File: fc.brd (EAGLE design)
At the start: 55 x 40 mm, 72 parts, among them IC1 BN055, J1 USBC, U1 LMZ21700, U2 ATMEGA2560-16AU100A-M, U4 FT230XQ, Y1 16MHz, Y2 32.768kHz

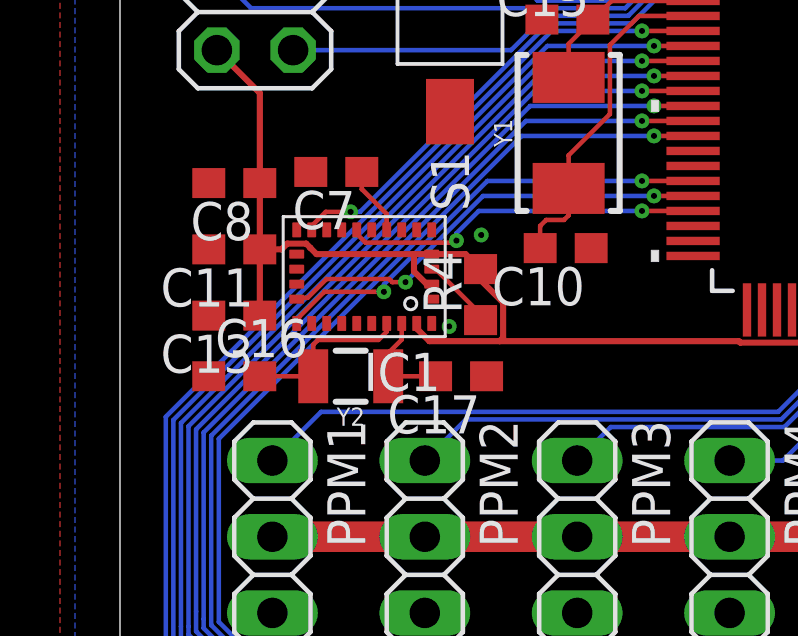
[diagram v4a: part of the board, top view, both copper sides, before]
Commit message: changed caps to sparkfun lib
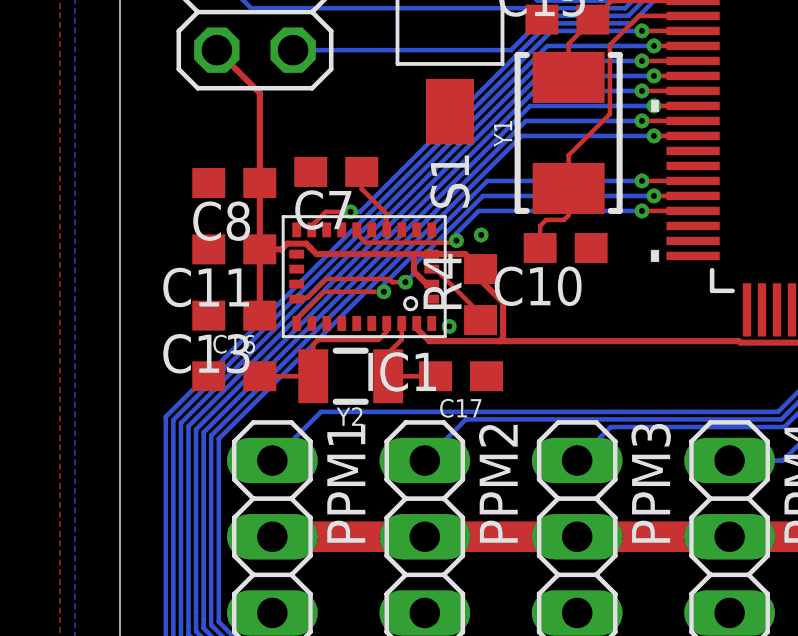
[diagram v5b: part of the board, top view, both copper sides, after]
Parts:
- C10, C12, C15, C4, C5, C6, C9: device rcl:C0603 -> sparkfun-generic-cap:0603
- C11, C13: device resistor:C0603 -> sparkfun-generic-cap:0603
- C16, C17: value 22p -> 22pF; device resistor:C0603 -> SparkFun-Capacitors:0603
- C7, C8: value 100n -> 0.1uF; device resistor:C0603 -> SparkFun-Capacitors:0603

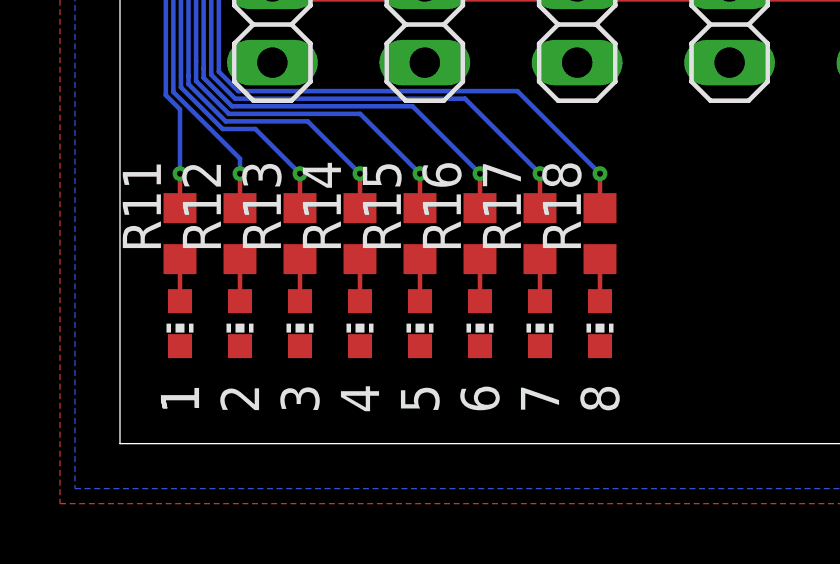
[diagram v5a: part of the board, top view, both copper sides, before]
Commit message: changed LEDs to sparkfun lib
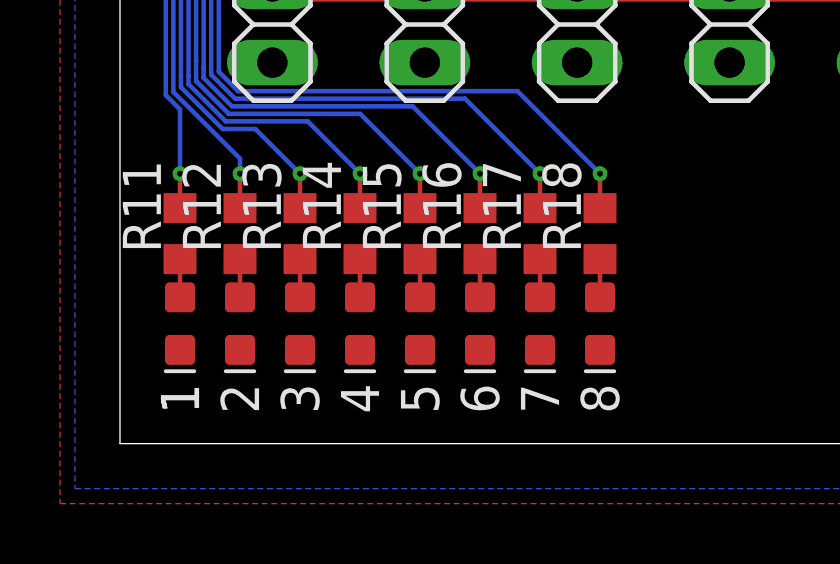
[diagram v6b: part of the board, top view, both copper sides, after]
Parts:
- LED1, LED2, LED3, LED4, LED5, LED6, LED7, LED8: device led:CHIP-LED0603 -> SparkFun-LED:LED-0603
- turned LED1 to 270 degrees
- turned LED2 to 270 degrees
- turned LED3 to 270 degrees
- turned LED4 to 270 degrees
- turned LED5 to 270 degrees
- turned LED6 to 270 degrees
- turned LED7 to 270 degrees
- turned LED8 to 270 degrees
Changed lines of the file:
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@@
 <attribute name="VALUE" x="7.905" y="6.365" size="1.27" layer="27" rot="R90"/>
 </element>
-<element name="LED1" library="led" library_urn="urn:adsk.eagle:library:259" package="CHIP-LED0603" package3d_urn="urn:adsk.eagle:package:15819/3" value="" x="2" y="4" smashed="yes" rot="R180">
-<attribute name="VALUE" x="0.095" y="4.635" size="1.27" layer="27" rot="R270"/>
+<element name="LED1" library="SparkFun-LED" library_urn="urn:adsk.eagle:library:529" package="LED-0603" package3d_urn="urn:adsk.eagle:package:39354/1" value="" x="2" y="4" smashed="yes" rot="R270">
+<attribute name="VALUE" x="1.365" y="2.095" size="1.27" layer="27"/>
 </element>
 <element name="R12" library="rcl" library_urn="urn:adsk.eagle:library:334" package="R0603" package3d_urn="urn:adsk.eagle:package:23555/2" value="100" x="4" y="7" smashed="yes" rot="R90">
@@
 <attribute name="VALUE" x="5.905" y="6.365" size="1.27" layer="27" rot="R90"/>
 </element>
-<element name="LED2" library="led" library_urn="urn:adsk.eagle:library:259" package="CHIP-LED0603" package3d_urn="urn:adsk.eagle:package:15819/3" value="" x="4" y="4" smashed="yes" rot="R180">
-<attribute name="VALUE" x="2.095" y="4.635" size="1.27" layer="27" rot="R270"/>
+<element name="LED2" library="SparkFun-LED" library_urn="urn:adsk.eagle:library:529" package="LED-0603" package3d_urn="urn:adsk.eagle:package:39354/1" value="" x="4" y="4" smashed="yes" rot="R270">
+<attribute name="VALUE" x="3.365" y="2.095" size="1.27" layer="27"/>
 </element>
 <element name="R13" library="rcl" library_urn="urn:adsk.eagle:library:334" package="R0603" package3d_urn="urn:adsk.eagle:package:23555/2" value="100" x="6" y="7" smashed="yes" rot="R90">
@@
 <attribute name="VALUE" x="7.905" y="6.365" size="1.27" layer="27" rot="R90"/>
 </element>
-<element name="LED3" library="led" library_urn="urn:adsk.eagle:library:259" package="CHIP-LED0603" package3d_urn="urn:adsk.eagle:package:15819/3" value="" x="6" y="4" smashed="yes" rot="R180">
-<attribute name="VALUE" x="4.095" y="4.635" size="1.27" layer="27" rot="R270"/>
+<element name="LED3" library="SparkFun-LED" library_urn="urn:adsk.eagle:library:529" package="LED-0603" package3d_urn="urn:adsk.eagle:package:39354/1" value="" x="6" y="4" smashed="yes" rot="R270">
+<attribute name="VALUE" x="5.365" y="2.095" size="1.27" layer="27"/>
 </element>
 <element name="R14" library="rcl" library_urn="urn:adsk.eagle:library:334" package="R0603" package3d_urn="urn:adsk.eagle:package:23555/2" value="100" x="8" y="7" smashed="yes" rot="R90">
@@
 <attribute name="VALUE" x="9.905" y="6.365" size="1.27" layer="27" rot="R90"/>
 </element>
-<element name="LED4" library="led" library_urn="urn:adsk.eagle:library:259" package="CHIP-LED0603" package3d_urn="urn:adsk.eagle:package:15819/3" value="" x="8" y="4" smashed="yes" rot="R180">
-<attribute name="VALUE" x="6.095" y="4.635" size="1.27" layer="27" rot="R270"/>
+<element name="LED4" library="SparkFun-LED" library_urn="urn:adsk.eagle:library:529" package="LED-0603" package3d_urn="urn:adsk.eagle:package:39354/1" value="" x="8" y="4" smashed="yes" rot="R270">
+<attribute name="VALUE" x="7.365" y="2.095" size="1.27" layer="27"/>
 </element>
 <element name="R15" library="rcl" library_urn="urn:adsk.eagle:library:334" package="R0603" package3d_urn="urn:adsk.eagle:package:23555/2" value="100" x="10" y="7" smashed="yes" rot="R90">
@@
 <attribute name="VALUE" x="11.905" y="6.365" size="1.27" layer="27" rot="R90"/>
 </element>
-<element name="LED5" library="led" library_urn="urn:adsk.eagle:library:259" package="CHIP-LED0603" package3d_urn="urn:adsk.eagle:package:15819/3" value="" x="10" y="4" smashed="yes" rot="R180">
-<attribute name="VALUE" x="8.095" y="4.635" size="1.27" layer="27" rot="R270"/>
+<element name="LED5" library="SparkFun-LED" library_urn="urn:adsk.eagle:library:529" package="LED-0603" package3d_urn="urn:adsk.eagle:package:39354/1" value="" x="10" y="4" smashed="yes" rot="R270">
+<attribute name="VALUE" x="9.365" y="2.095" size="1.27" layer="27"/>
 </element>
 <element name="R16" library="rcl" library_urn="urn:adsk.eagle:library:334" package="R0603" package3d_urn="urn:adsk.eagle:package:23555/2" value="100" x="12" y="7" smashed="yes" rot="R90">
@@
 <attribute name="VALUE" x="13.905" y="6.365" size="1.27" layer="27" rot="R90"/>
 </element>
-<element name="LED6" library="led" library_urn="urn:adsk.eagle:library:259" package="CHIP-LED0603" package3d_urn="urn:adsk.eagle:package:15819/3" value="" x="12" y="4" smashed="yes" rot="R180">
-<attribute name="VALUE" x="10.095" y="4.635" size="1.27" layer="27" rot="R270"/>
+<element name="LED6" library="SparkFun-LED" library_urn="urn:adsk.eagle:library:529" package="LED-0603" package3d_urn="urn:adsk.eagle:package:39354/1" value="" x="12" y="4" smashed="yes" rot="R270">
+<attribute name="VALUE" x="11.365" y="2.095" size="1.27" layer="27"/>
 </element>
 <element name="R17" library="rcl" library_urn="urn:adsk.eagle:library:334" package="R0603" package3d_urn="urn:adsk.eagle:package:23555/2" value="100" x="14" y="7" smashed="yes" rot="R90">
@@
 <attribute name="VALUE" x="15.905" y="6.365" size="1.27" layer="27" rot="R90"/>
 </element>
-<element name="LED7" library="led" library_urn="urn:adsk.eagle:library:259" package="CHIP-LED0603" package3d_urn="urn:adsk.eagle:package:15819/3" value="" x="14" y="4" smashed="yes" rot="R180">
-<attribute name="VALUE" x="12.095" y="4.635" size="1.27" layer="27" rot="R270"/>
+<element name="LED7" library="SparkFun-LED" library_urn="urn:adsk.eagle:library:529" package="LED-0603" package3d_urn="urn:adsk.eagle:package:39354/1" value="" x="14" y="4" smashed="yes" rot="R270">
+<attribute name="VALUE" x="13.365" y="2.095" size="1.27" layer="27"/>
 </element>
 <element name="R18" library="rcl" library_urn="urn:adsk.eagle:library:334" package="R0603" package3d_urn="urn:adsk.eagle:package:23555/2" value="100" x="16" y="7" smashed="yes" rot="R90">
@@
 <attribute name="VALUE" x="17.905" y="6.365" size="1.27" layer="27" rot="R90"/>
 </element>
-<element name="LED8" library="led" library_urn="urn:adsk.eagle:library:259" package="CHIP-LED0603" package3d_urn="urn:adsk.eagle:package:15819/3" value="" x="16" y="4" smashed="yes" rot="R180">
-<attribute name="VALUE" x="14.095" y="4.635" size="1.27" layer="27" rot="R270"/>
+<element name="LED8" library="SparkFun-LED" library_urn="urn:adsk.eagle:library:529" package="LED-0603" package3d_urn="urn:adsk.eagle:package:39354/1" value="" x="16" y="4" smashed="yes" rot="R270">
+<attribute name="VALUE" x="15.365" y="2.095" size="1.27" layer="27"/>
 </element>
 <element name="JP1" library="pinhead" library_urn="urn:adsk.eagle:library:325" package="1X03" package3d_urn="urn:adsk.eagle:package:22458/2" value="" x="47.868" y="36.4904" smashed="yes" rot="R180">
@@
 <contactref element="R11" pad="1"/>
 <contactref element="LED1" pad="A"/>
-<wire x1="2" y1="6.15" x2="2" y2="4.75" width="0.1524" layer="1"/>
+<wire x1="2" y1="6.15" x2="2" y2="4.877" width="0.1524" layer="1"/>
 </signal>
 <signal name="LED0">
@@
 <contactref element="R12" pad="1"/>
 <contactref element="LED2" pad="A"/>
-<wire x1="4" y1="4.75" x2="4" y2="6.15" width="0.1524" layer="1"/>
+<wire x1="4" y1="4.877" x2="4" y2="6.15" width="0.1524" layer="1"/>
 </signal>
 <signal name="N$18">
 <contactref element="R13" pad="1"/>
 <contactref element="LED3" pad="A"/>
-<wire x1="6" y1="4.75" x2="6" y2="6.15" width="0.1524" layer="1"/>
+<wire x1="6" y1="4.877" x2="6" y2="6.15" width="0.1524" layer="1"/>
 </signal>
 <signal name="N$20">
 <contactref element="R14" pad="1"/>
 <contactref element="LED4" pad="A"/>
-<wire x1="8" y1="4.75" x2="8" y2="6.15" width="0.1524" layer="1"/>
+<wire x1="8" y1="4.877" x2="8" y2="6.15" width="0.1524" layer="1"/>
 </signal>
 <signal name="N$22">
 <contactref element="R15" pad="1"/>
 <contactref element="LED5" pad="A"/>
-<wire x1="10" y1="4.75" x2="10" y2="6.15" width="0.1524" layer="1"/>
+<wire x1="10" y1="4.877" x2="10" y2="6.15" width="0.1524" layer="1"/>
 </signal>
 <signal name="N$24">
 <contactref element="R16" pad="1"/>
 <contactref element="LED6" pad="A"/>
-<wire x1="12" y1="4.75" x2="12" y2="6.15" width="0.1524" layer="1"/>
+<wire x1="12" y1="4.877" x2="12" y2="6.15" width="0.1524" layer="1"/>
 </signal>
 <signal name="N$27">
 <contactref element="R17" pad="1"/>
 <contactref element="LED7" pad="A"/>
-<wire x1="14" y1="4.75" x2="14" y2="6.15" width="0.1524" layer="1"/>
+<wire x1="14" y1="4.877" x2="14" y2="6.15" width="0.1524" layer="1"/>
 </signal>
 <signal name="N$29">
 <contactref element="R18" pad="1"/>
 <contactref element="LED8" pad="A"/>
-<wire x1="16" y1="4.75" x2="16" y2="6.15" width="0.1524" layer="1"/>
+<wire x1="16" y1="4.877" x2="16" y2="6.15" width="0.1524" layer="1"/>
 </signal>
 <signal name="MISO">

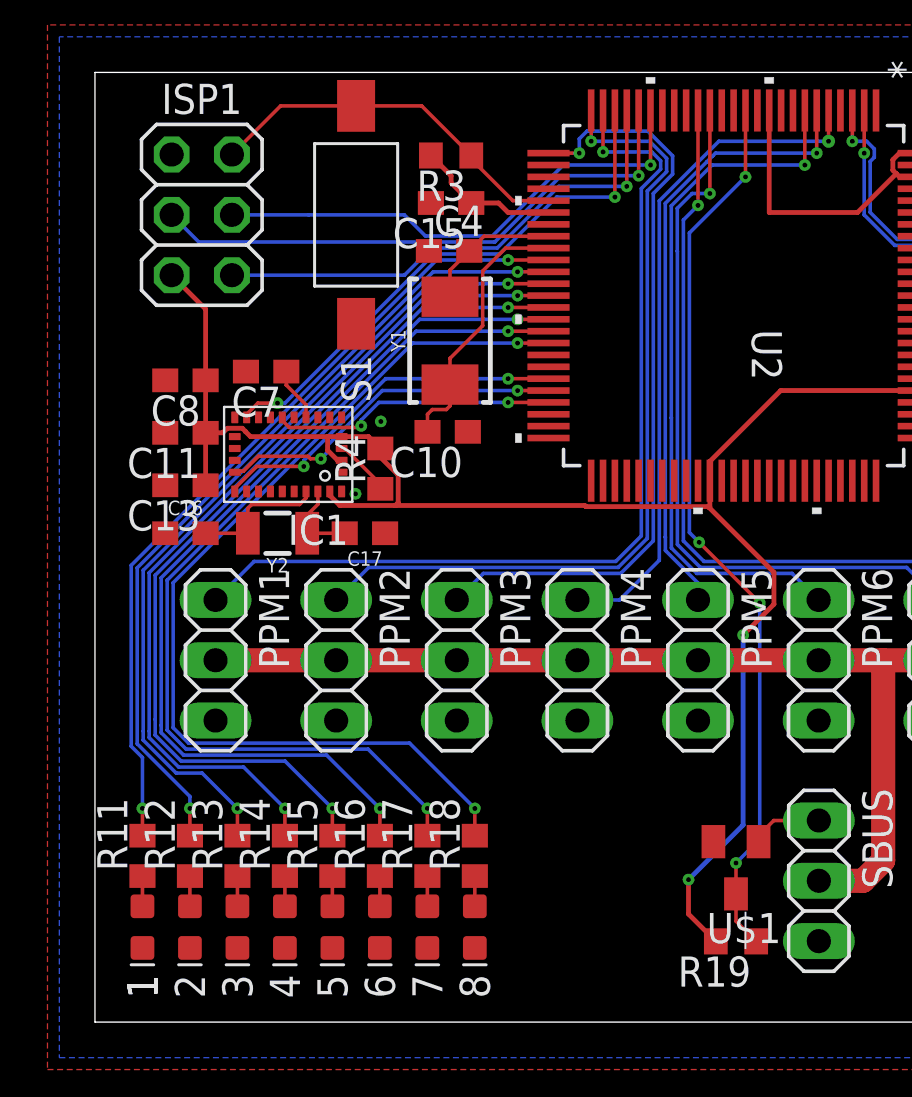
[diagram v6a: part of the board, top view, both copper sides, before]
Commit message: changed resistors to sparkfun lib
how nice, all the 0603 parts are the same size now.
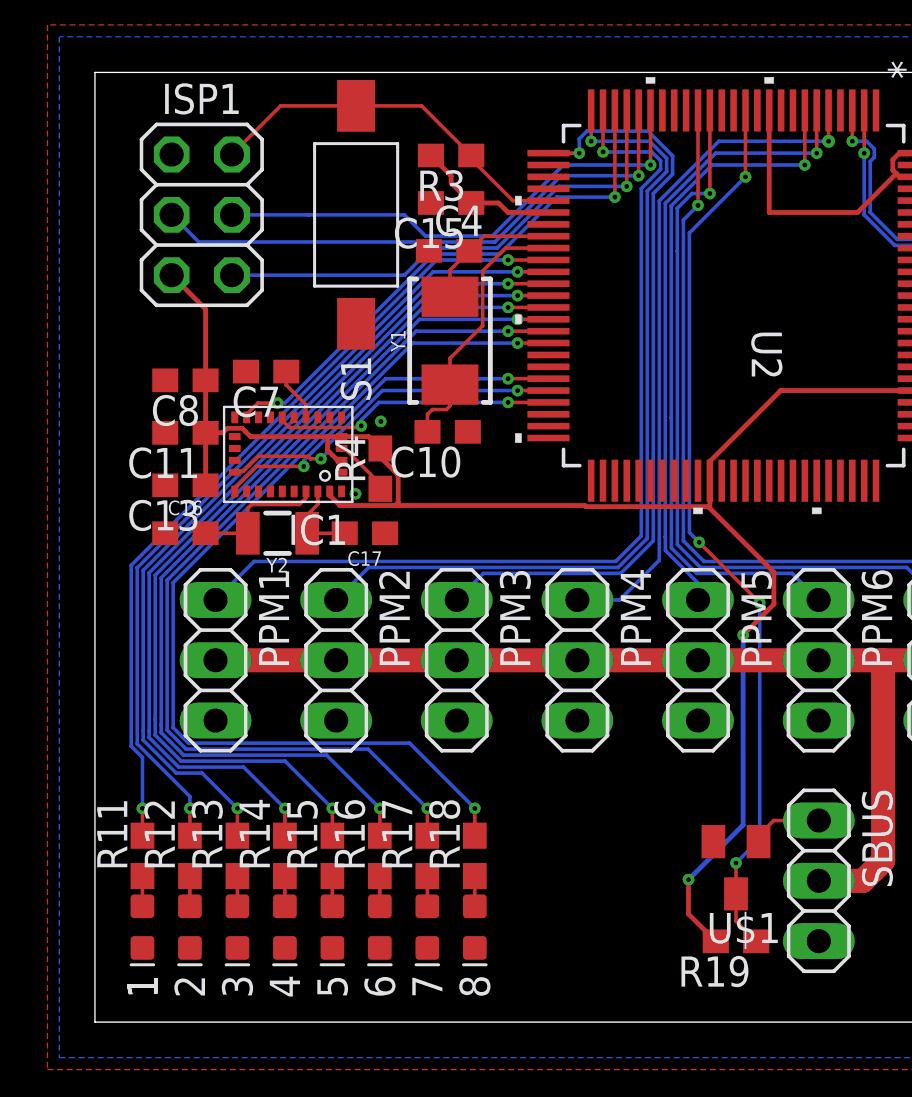
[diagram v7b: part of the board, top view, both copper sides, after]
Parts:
- R11, R12, R13, R14, R15, R16, R17, R18: device rcl:R0603 -> SparkFun-Resistors:0603
- R19: value (none) -> 4.7k; device resistor:R0603 -> SparkFun-Resistors:0603
- R3, R4: device resistor:R0603 -> SparkFun-Resistors:0603

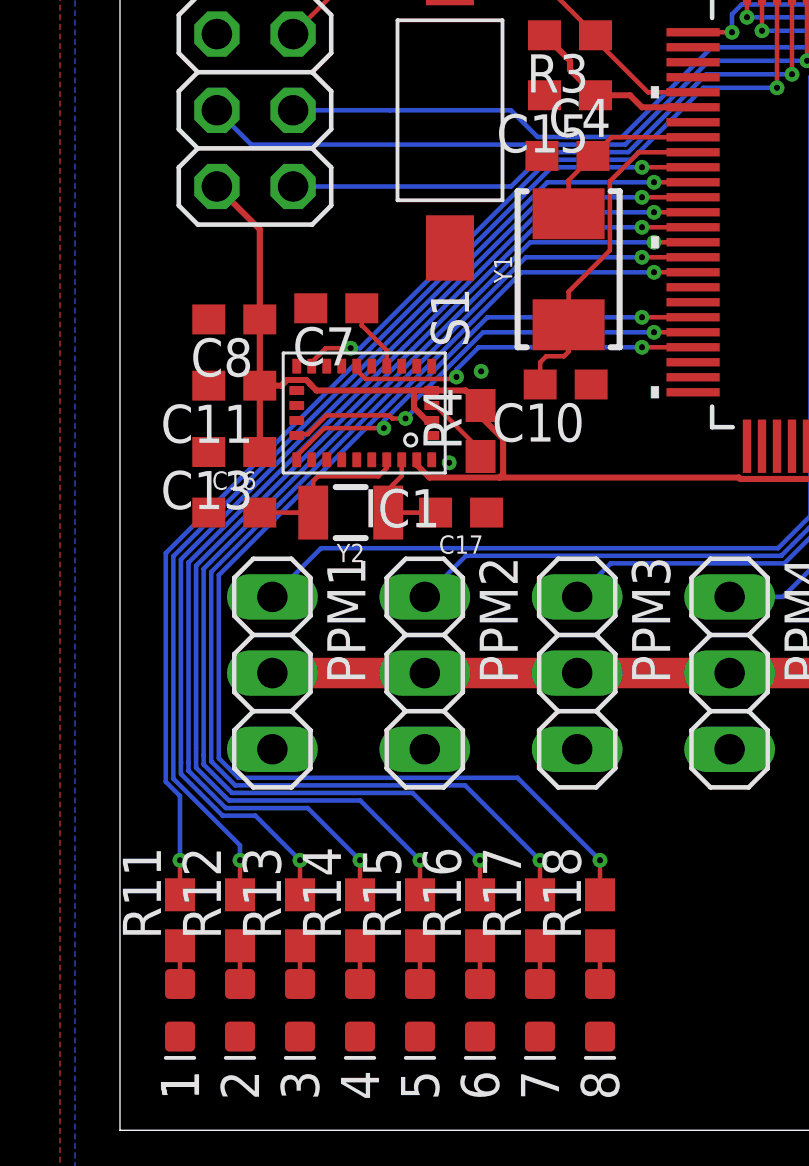
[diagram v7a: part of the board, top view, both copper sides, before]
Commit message: move led resistors up
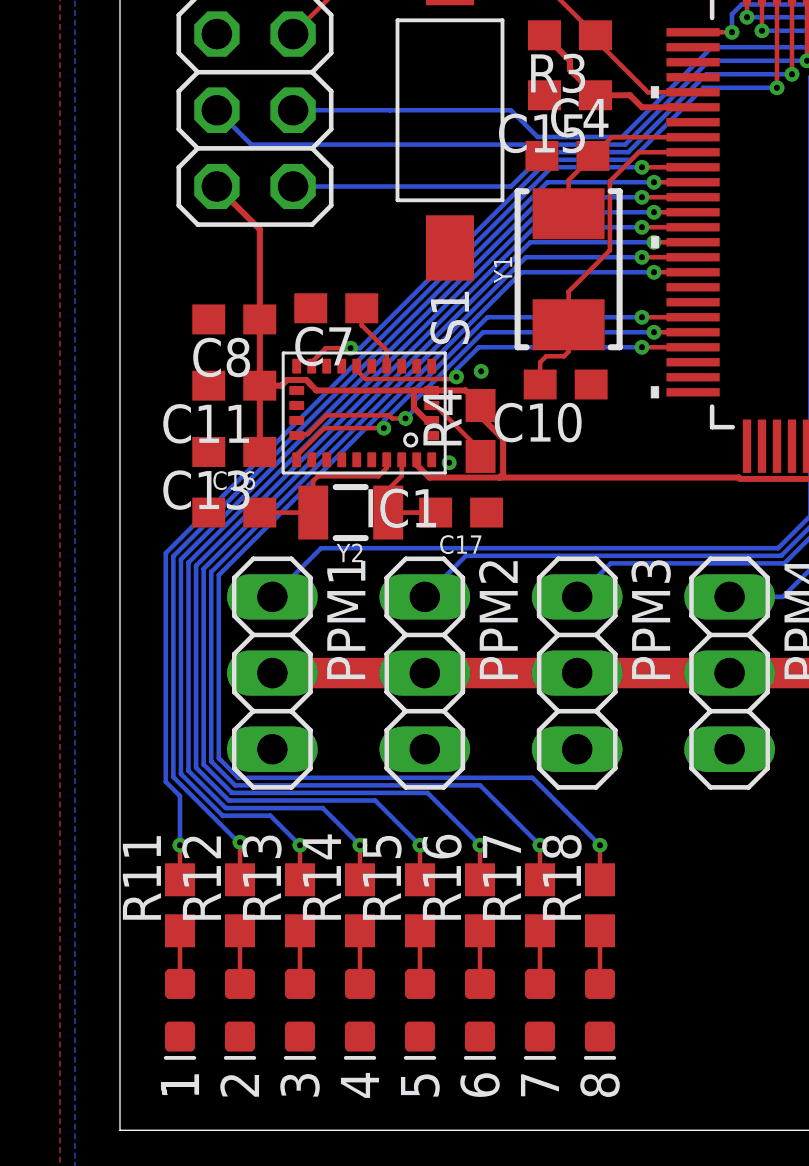
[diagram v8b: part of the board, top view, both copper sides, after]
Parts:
- moved R11 0.50 mm to (2.00, 7.50)
- moved R12 0.50 mm to (4.00, 7.50)
- moved R13 0.50 mm to (6.00, 7.50)
- moved R14 0.50 mm to (8.00, 7.50)
- moved R15 0.50 mm to (10.0, 7.50)
- moved R16 0.50 mm to (12.0, 7.50)
- moved R17 0.50 mm to (14.0, 7.50)
- moved R18 0.50 mm to (16.0, 7.50)
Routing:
- net N$31: track 1.27 -> 1.77 mm
- net N$29: track 1.27 -> 1.77 mm
- net N$27: track 1.27 -> 1.77 mm
- net N$24: track 1.27 -> 1.77 mm
- net N$22: track 1.27 -> 1.77 mm
- net N$20: track 1.27 -> 1.77 mm
- net N$18: track 1.27 -> 1.77 mm
- net N$15: track 1.27 -> 1.77 mm
- net LED0: track 34.5 -> 34.0 mm
